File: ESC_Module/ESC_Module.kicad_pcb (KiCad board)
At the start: 2 copper layers, 53.5 x 30 mm, 4 parts, among them P1 CONN_02X04, P2 CONN_02X04, U1 DYS_mini_ESC

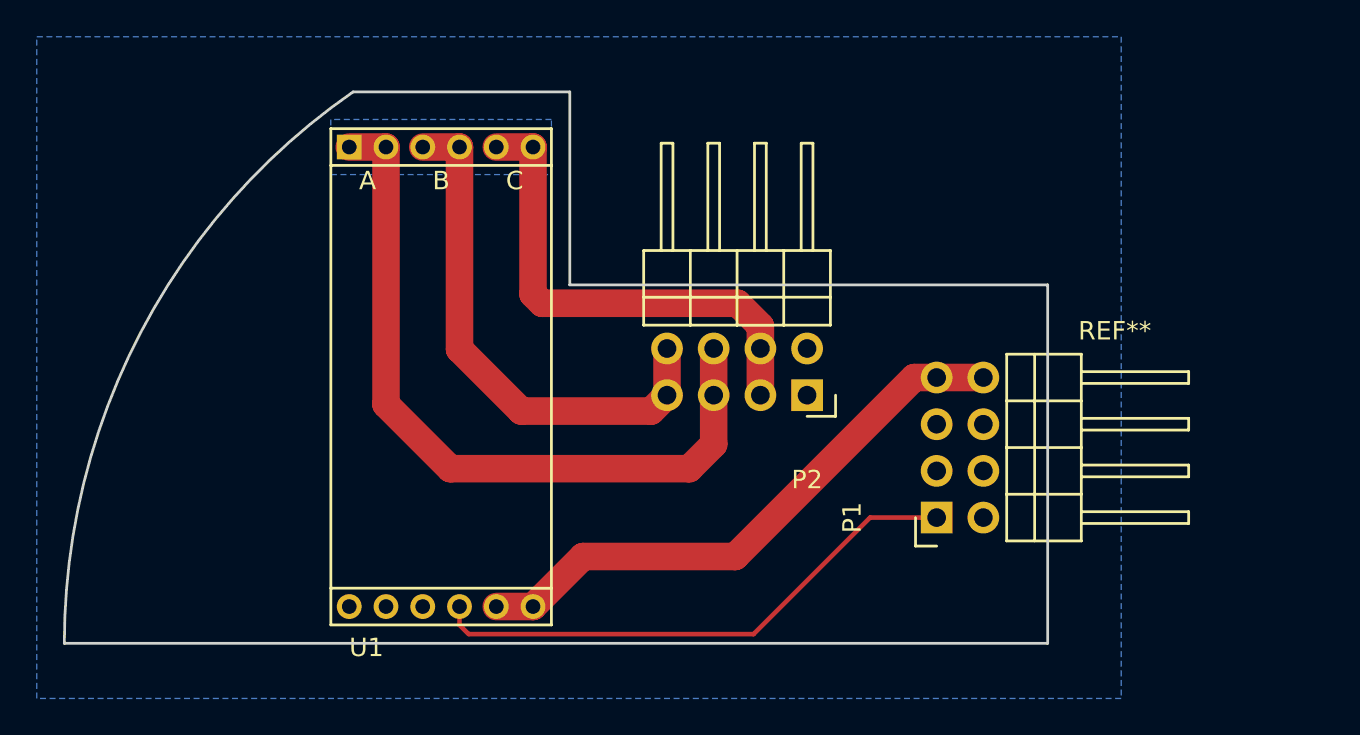
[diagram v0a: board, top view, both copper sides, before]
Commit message: Resize PCBs
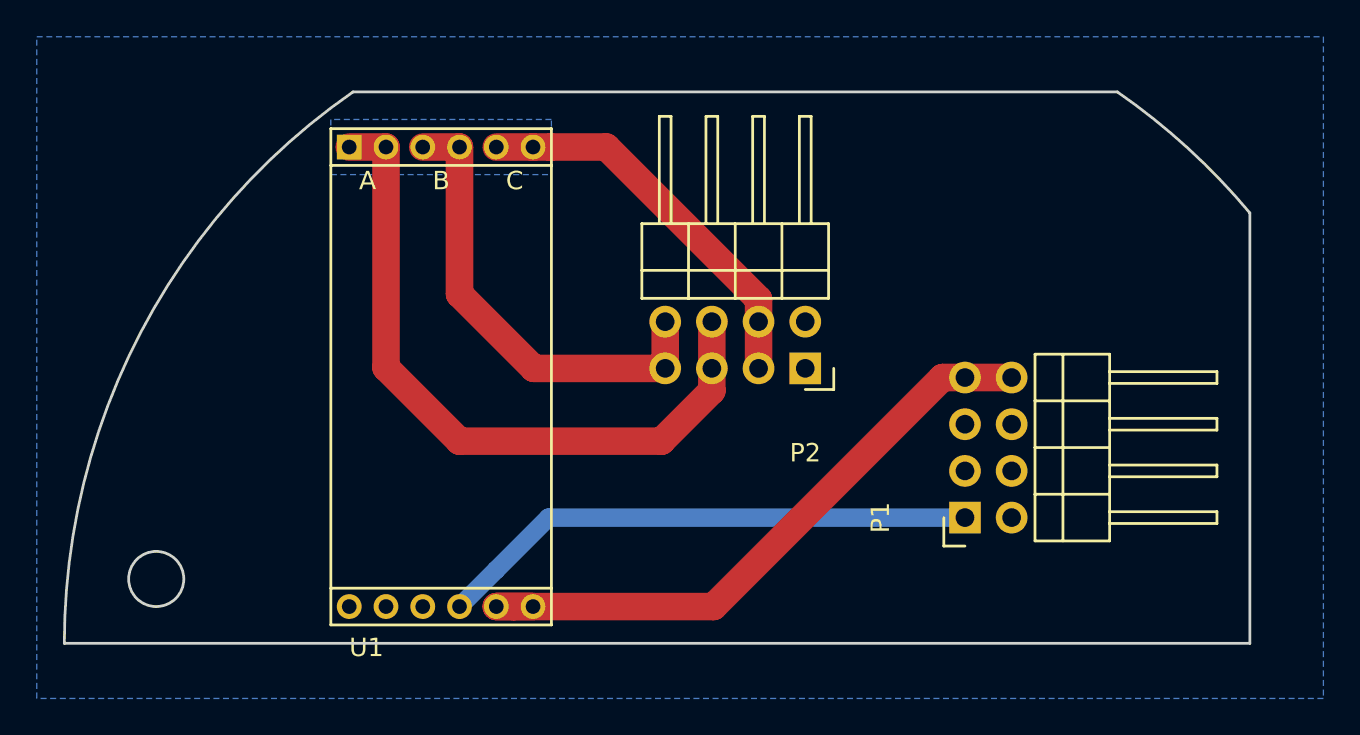
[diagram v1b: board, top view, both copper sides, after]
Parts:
- removed REF**: 02x06_pin_header_Socket, KiCad_Footprint:02x06_pin_header_Socket
- moved P1 1.54 mm to (112.5, 93.2)
- moved P2 1.46 mm to (103.8, 85.0)
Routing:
- net /OUT_C: track 26.9 -> 21.5 mm
- net /V_BAT: track 31.7 -> 35.2 mm
- net /OUT_B: track 28.6 -> 25.4 mm
- net /OUT_A: track 41.0 -> 38.3 mm
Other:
- board size 53.5 x 30 mm -> 64.5 x 30 mm
- net class Default: trace_width 0.25 -> 1
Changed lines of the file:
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@@
     (links 19)
     (no_connects 0)
-    (area 63.424999 69.924999 117.075001 100.075001)
+    (area 63.424999 69.924999 128.075001 100.075001)
     (thickness 1.6)
     (drawings 6)
-    (tracks 31)
+    (tracks 27)
     (zones 0)
-    (modules 4)
+    (modules 3)
     (nets 7)
   )
@@
   )
   (setup
-    (last_trace_width 0.25)
+    (last_trace_width 1)
     (trace_clearance 0.2)
     (zone_clearance 0.508)
@@
   (net_class Default "This is the default net class."
     (clearance 0.2)
-    (trace_width 0.25)
+    (trace_width 1)
     (via_dia 0.6)
     (via_drill 0.4)
@@
     )
   )
-  (module KiCad_Footprint:02x06_pin_header_Socket locked (layer F.Cu)
-    (at 128.27 84.02)
-    (fp_text reference REF** (at -7.62 -1.016) (layer F.SilkS)
-      (effects (font (size 1 1) (thickness 0.15)))
-    )
-    (fp_text value 02x06_pin_header_Socket (at -4.572 17.272) (layer F.Fab)
-      (effects (font (size 1 1) (thickness 0.15)))
-    )
-    (fp_line (start -2.5 1.02) (end -2.5 2.02) (layer B.Paste) (width 0.15))
-    (fp_line (start -2.5 2.02) (end -8.5 2.02) (layer B.Paste) (width 0.15))
-    (fp_line (start -8.5 1.02) (end -2.5 1.02) (layer B.Paste) (width 0.15))
-    (fp_line (start -8.5 0) (end 0 0) (layer B.Paste) (width 0.15))
-    (fp_line (start -8.5 15.74) (end -8.5 0) (layer B.Paste) (width 0.15))
-    (fp_line (start -8.5 15.74) (end 0 15.74) (layer B.Paste) (width 0.15))
-    (fp_line (start 0 0) (end 0 15.74) (layer B.Paste) (width 0.15))
-    (fp_line (start -8.5 3.56) (end -2.5 3.56) (layer B.Paste) (width 0.15))
-    (fp_line (start -8.5 6.1) (end -2.5 6.1) (layer B.Paste) (width 0.15))
-    (fp_line (start -8.5 8.64) (end -2.5 8.64) (layer B.Paste) (width 0.15))
-    (fp_line (start -8.5 11.18) (end -2.5 11.18) (layer B.Paste) (width 0.15))
-    (fp_line (start -8.5 13.72) (end -2.5 13.72) (layer B.Paste) (width 0.15))
-    (fp_line (start -2.5 3.56) (end -2.5 4.56) (layer B.Paste) (width 0.15))
-    (fp_line (start -2.5 6.1) (end -2.5 7.1) (layer B.Paste) (width 0.15))
-    (fp_line (start -2.5 8.64) (end -2.5 9.64) (layer B.Paste) (width 0.15))
-    (fp_line (start -2.5 11.18) (end -2.5 12.18) (layer B.Paste) (width 0.15))
-    (fp_line (start -2.5 13.72) (end -2.5 14.72) (layer B.Paste) (width 0.15))
-    (fp_line (start -2.5 4.56) (end -8.5 4.56) (layer B.Paste) (width 0.15))
-    (fp_line (start -2.5 7.1) (end -8.5 7.1) (layer B.Paste) (width 0.15))
-    (fp_line (start -2.5 9.64) (end -8.5 9.64) (layer B.Paste) (width 0.15))
-    (fp_line (start -2.5 12.18) (end -8.5 12.18) (layer B.Paste) (width 0.15))
-    (fp_line (start -2.5 14.72) (end -8.5 14.72) (layer B.Paste) (width 0.15))
-  )
-  (module KiCad_Footprint:Socket_Strip_Angled_2x04 locked (layer F.Cu)
-    (at 103.91 86.5 180)
+  (module KiCad_Footprint:Socket_Strip_Angled_2x04 (layer F.Cu)
+    (at 103.81 85.04 180)
     (descr "Through hole socket strip")
     (tags "socket strip")
@@
   )
   (module KiCad_Footprint:Socket_Strip_Angled_2x04 locked (layer F.Cu)
-    (at 110.96 93.16 90)
+    (at 112.5 93.16 90)
     (descr "Through hole socket strip")
     (tags "socket strip")
@@
     )
   )
-  (gr_line (start 91 70) (end 79.209377 70) (layer Edge.Cuts) (width 0.15))
-  (gr_line (start 91 80.5) (end 91 70) (layer Edge.Cuts) (width 0.15))
-  (gr_line (start 117 80.5) (end 91 80.5) (layer Edge.Cuts) (width 0.15))
-  (gr_arc (start 100 100) (end 63.5 100) (angle 55.27723707) (layer Edge.Cuts) (width 0.15))
-  (gr_line (start 117 100) (end 63.5 100) (layer Edge.Cuts) (width 0.15))
-  (gr_line (start 117 100) (end 117 80.5) (layer Edge.Cuts) (width 0.15))
+  (gr_circle (center 68.5 96.5) (end 68.5 98) (layer Edge.Cuts) (width 0.15))
+  (gr_arc (start 100 100) (end 63.5 100) (angle 55.2772371) (layer Edge.Cuts) (width 0.15))
+  (gr_arc (start 100 100) (end 128 76.585261) (angle -15.3734978) (layer Edge.Cuts) (width 0.15))
+  (gr_line (start 128 100) (end 128 76.585261) (layer Edge.Cuts) (width 0.15))
+  (gr_line (start 120.790623 70) (end 79.209377 70) (layer Edge.Cuts) (width 0.15))
+  (gr_line (start 128 100) (end 63.5 100) (layer Edge.Cuts) (width 0.15))
+  (segment (start 112.5 85.54) (end 111.278686 85.54) (width 1.5) (layer F.Cu) (net 1))
+  (segment (start 111.278686 85.54) (end 98.818686 98) (width 1.5) (layer F.Cu) (net 1))
+  (segment (start 98.818686 98) (end 87.954594 98) (width 1.5) (layer F.Cu) (net 1))
+  (segment (start 87.954594 98) (end 87 98) (width 1.5) (layer F.Cu) (net 1))
+  (segment (start 115.04 85.54) (end 112.5 85.54) (width 1.5) (layer F.Cu) (net 1))
   (segment (start 89 98) (end 87 98) (width 1.5) (layer F.Cu) (net 1))
-  (segment (start 110.96 85.54) (end 109.738686 85.54) (width 1.5) (layer F.Cu) (net 1))
-  (segment (start 109.738686 85.54) (end 100 95.278686) (width 1.5) (layer F.Cu) (net 1))
-  (segment (start 100 95.278686) (end 91.721314 95.278686) (width 1.5) (layer F.Cu) (net 1))
-  (segment (start 91.721314 95.278686) (end 89 98) (width 1.5) (layer F.Cu) (net 1))
-  (segment (start 113.5 85.54) (end 110.96 85.54) (width 1.5) (layer F.Cu) (net 1))
+  (segment (start 101.27 82.5) (end 101.27 81.278686) (width 1.5) (layer F.Cu) (net 3))
+  (segment (start 101.27 81.278686) (end 92.991314 73) (width 1.5) (layer F.Cu) (net 3))
+  (segment (start 92.991314 73) (end 89.954594 73) (width 1.5) (layer F.Cu) (net 3))
+  (segment (start 89.954594 73) (end 89 73) (width 1.5) (layer F.Cu) (net 3))
+  (segment (start 101.27 85.04) (end 101.27 82.5) (width 1.5) (layer F.Cu) (net 3))
   (segment (start 89 73) (end 87 73) (width 1.5) (layer F.Cu) (net 3))
-  (segment (start 101.37 83.96) (end 101.37 82.738686) (width 1.5) (layer F.Cu) (net 3))
-  (segment (start 101.37 82.738686) (end 100.131314 81.5) (width 1.5) (layer F.Cu) (net 3))
-  (segment (start 100.131314 81.5) (end 89.5 81.5) (width 1.5) (layer F.Cu) (net 3))
-  (segment (start 89.5 81.5) (end 89 81) (width 1.5) (layer F.Cu) (net 3))
-  (segment (start 89 81) (end 89 73) (width 1.5) (layer F.Cu) (net 3))
-  (segment (start 101.37 86.5) (end 101.37 83.96) (width 1.5) (layer F.Cu) (net 3))
+  (segment (start 96.19 85.04) (end 96.19 82.5) (width 1.5) (layer F.Cu) (net 4))
+  (segment (start 85 73) (end 85 81) (width 1.5) (layer F.Cu) (net 4))
+  (segment (start 89.04 85.04) (end 96.19 85.04) (width 1.5) (layer F.Cu) (net 4))
+  (segment (start 85 81) (end 89.04 85.04) (width 1.5) (layer F.Cu) (net 4))
   (segment (start 85 73) (end 83 73) (width 1.5) (layer F.Cu) (net 4))
-  (segment (start 88.363599 87.363599) (end 85 84) (width 1.5) (layer F.Cu) (net 4))
-  (segment (start 85 84) (end 85 73) (width 1.5) (layer F.Cu) (net 4))
-  (segment (start 96.29 86.5) (end 95.426401 87.363599) (width 1.5) (layer F.Cu) (net 4))
-  (segment (start 95.426401 87.363599) (end 88.363599 87.363599) (width 1.5) (layer F.Cu) (net 4))
-  (segment (start 96.29 83.96) (end 96.29 86.5) (width 1.5) (layer F.Cu) (net 4))
-  (segment (start 81 73) (end 81 87) (width 1.5) (layer F.Cu) (net 5))
-  (segment (start 81 87) (end 84.5 90.5) (width 1.5) (layer F.Cu) (net 5))
-  (segment (start 84.5 90.5) (end 97.5 90.5) (width 1.5) (layer F.Cu) (net 5))
-  (segment (start 97.5 90.5) (end 98.83 89.17) (width 1.5) (layer F.Cu) (net 5))
-  (segment (start 98.83 89.17) (end 98.83 86.5) (width 1.5) (layer F.Cu) (net 5))
+  (segment (start 98.73 85.04) (end 98.73 82.5) (width 1.5) (layer F.Cu) (net 5))
+  (segment (start 85 89) (end 95.991314 89) (width 1.5) (layer F.Cu) (net 5))
+  (segment (start 95.991314 89) (end 98.73 86.261314) (width 1.5) (layer F.Cu) (net 5))
+  (segment (start 98.73 86.261314) (end 98.73 85.04) (width 1.5) (layer F.Cu) (net 5))
+  (segment (start 81 85) (end 85 89) (width 1.5) (layer F.Cu) (net 5))
+  (segment (start 81 73) (end 81 85) (width 1.5) (layer F.Cu) (net 5))
   (segment (start 81 73) (end 79 73) (width 1.5) (layer F.Cu) (net 5))
-  (segment (start 98.83 83.96) (end 98.83 86.5) (width 1.5) (layer F.Cu) (net 5))
-  (segment (start 110.96 93.16) (end 107.34 93.16) (width 0.25) (layer F.Cu) (net 6))
-  (segment (start 85 99) (end 85 98) (width 0.25) (layer F.Cu) (net 6))
-  (segment (start 85.5 99.5) (end 85 99) (width 0.25) (layer F.Cu) (net 6))
-  (segment (start 101 99.5) (end 85.5 99.5) (width 0.25) (layer F.Cu) (net 6))
-  (segment (start 107.34 93.16) (end 101 99.5) (width 0.25) (layer F.Cu) (net 6))
+  (segment (start 87 96) (end 85 98) (width 1) (layer B.Cu) (net 6))
+  (segment (start 112.5 93.16) (end 89.84 93.16) (width 1) (layer B.Cu) (net 6))
+  (segment (start 89.84 93.16) (end 87 96) (width 1) (layer B.Cu) (net 6))
   (zone (net 2) (net_name GND) (layer B.Cu) (hatch edge 0.508)
     (connect_pads yes (clearance 0.508))
@@
     (polygon
       (pts
-        (xy 121 103) (xy 62 103) (xy 62 67) (xy 121 67)
+        (xy 132 103) (xy 62 103) (xy 62 67) (xy 132 67)
       )
     )

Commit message: Commit update
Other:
- outline, holes or cut-outs redrawn
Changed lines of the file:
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@@
     (links 19)
     (no_connects 0)
-    (area 63.424999 69.924999 128.075001 100.075001)
+    (area 62 67 132.000001 103.000001)
     (thickness 1.6)
     (drawings 6)
@@
     )
   )
-  (gr_circle (center 68.5 96.5) (end 68.5 98) (layer Edge.Cuts) (width 0.15))
+  (gr_circle (center 67 96.5) (end 67 98) (layer Edge.Cuts) (width 0.15))
   (gr_arc (start 100 100) (end 63.5 100) (angle 55.2772371) (layer Edge.Cuts) (width 0.15))
   (gr_arc (start 100 100) (end 128 76.585261) (angle -15.3734978) (layer Edge.Cuts) (width 0.15))

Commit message: modify..
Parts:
- added C1: 330uF, Capacitors_SMD:c_elec_8x10, F.Cu at (104.0, 92.8)
- moved U1 2.14 mm to (86.0, 84.8)
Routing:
- net /OUT_A: track 38.3 -> 25.9 mm
- net /V_BAT: track 35.2 -> 43.0 mm
- net /OUT_B: track 25.4 -> 19.6 mm
- net /PWM_Input: track 29.5 -> 33.5 mm
- net /OUT_C: track 21.5 -> 22.3 mm
- added copper zone on F.Cu, net GND
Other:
- net class Default: trace_width 1 -> 1.5
